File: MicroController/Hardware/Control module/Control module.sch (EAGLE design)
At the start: 90 parts, among them CN1 JST-PH_2-PIN_HEADER, CN2 JST-PH_2-PIN_HEADER, CN3 JST-PH_2-PIN_HEADER, CN4 JST-PH_2-PIN_HEADER, CN5 JST-PH_2-PIN_HEADER, CN6 JST-PH_2-PIN_HEADER, CN7 JST-PH_2-PIN_HEADER, CN8 JST-PH_2-PIN_HEADER, J1 1X2-3.5MM, J2 RJ45-TRAFO, J3 RJ45-TRAFO, J4 RJ45-TRAFO, J6 RJ11, Q1 BSS138, Q2 BSS138, Q3 BSS138, Q4 BSS138, Q5 BSS138, Q6 BSS138, Q7 BSS138, Q8 BSS138, U1 CD74HC4067SM96, U2 DUAL-OPTOISOLATOR_SOIC8, U3 TLV1117-33CDCY, U4 DUAL-OPTOISOLATOR_SOIC8

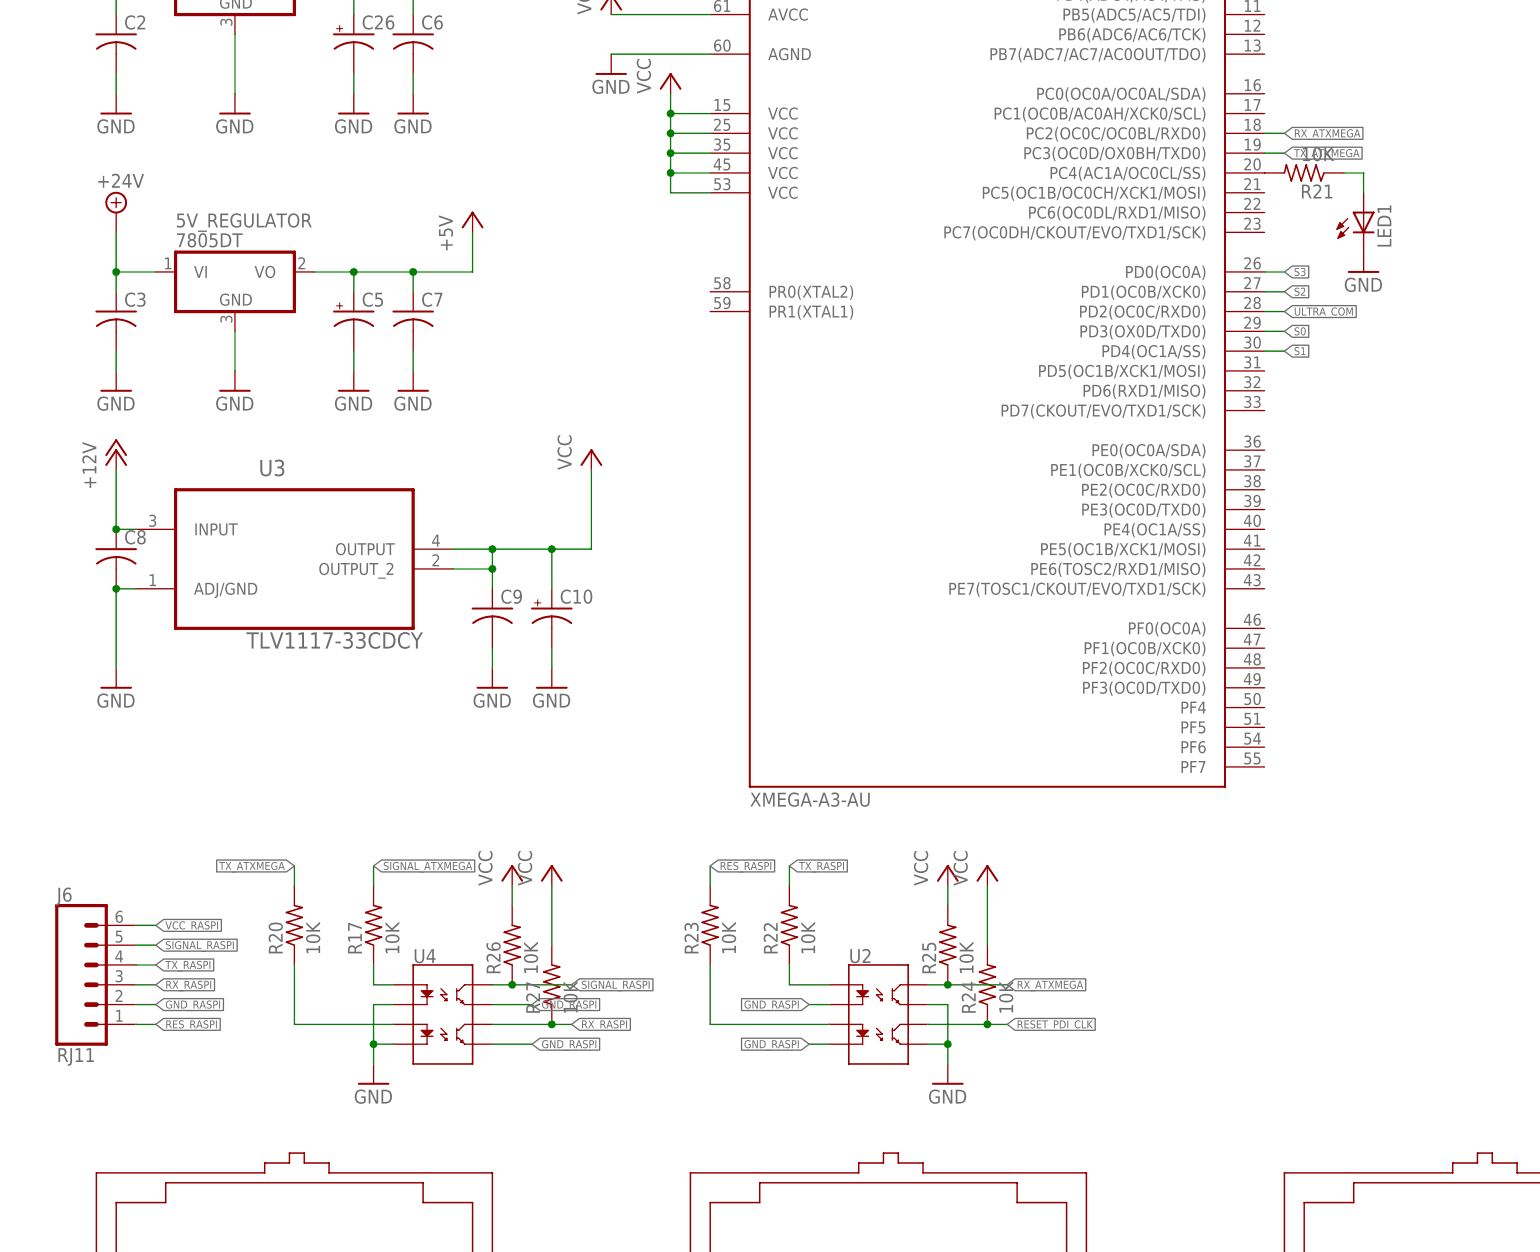
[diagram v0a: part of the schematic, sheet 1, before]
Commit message: Added the possibility for remote programming.
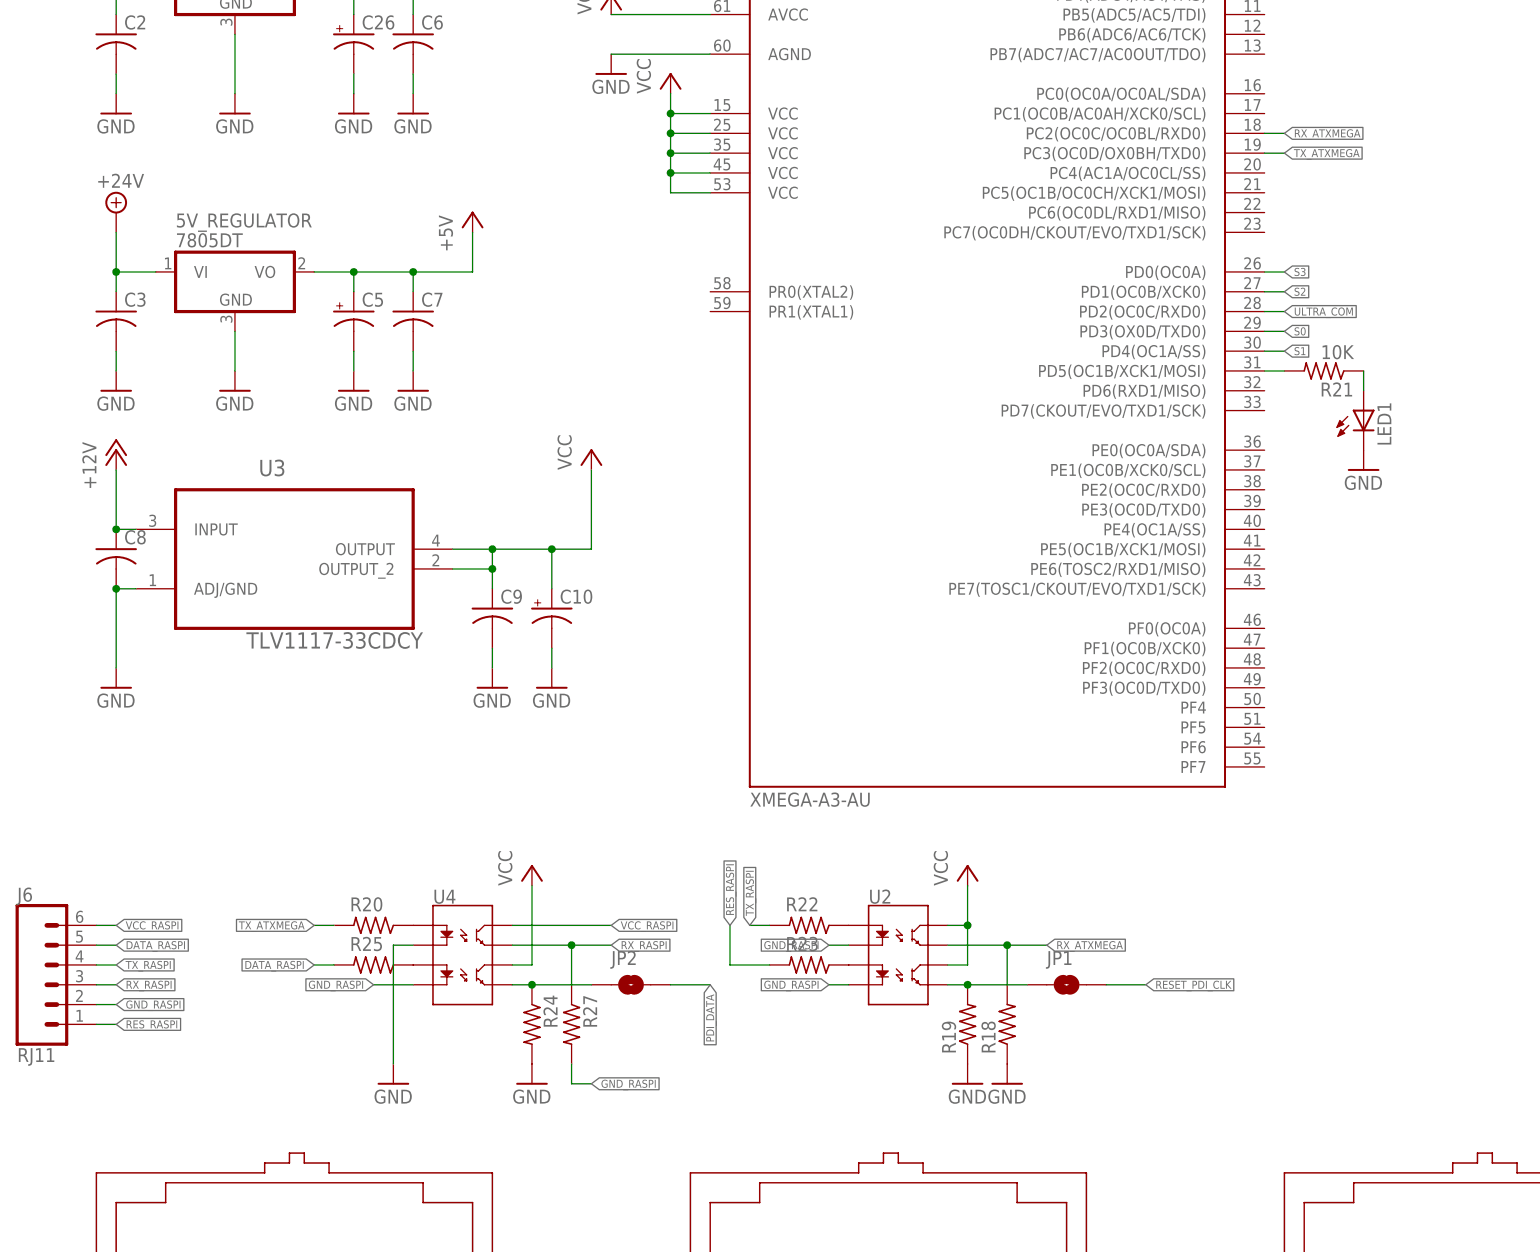
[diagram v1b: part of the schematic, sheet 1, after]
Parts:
- removed R17, R26: 10K, adafruit:R-US_R0805
- added JP1, JP2: JUMPER-SMT_2_NO_NO-SILK, SparkFun-Jumpers:JUMPER-SMT_2_NO_NO-SILK
- added R18, R19: 10K, adafruit:R-US_R0805
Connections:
- removed net N$3 (its old number): R21.2, U$1.PC4(AC1A/OC0CL/SS)
- removed net SIGNAL_ATXMEGA: R17.2
- removed net SIGNAL_RASPI: J6.5, R26.1, U4.CL1
- new net DATA_RASPI: J6.5, R25.2
- new net N$1: R21.2, U$1.PD5(OC1B/XCK1/MOSI)
- new net N$4: R20.1, U4.A1
- new net N$5: R25.1, U4.A2
- net GND: now also R18.1, R19.1, R24.2; no longer U2.EM1, U2.EM2, U4.C2
- net GND_RASPI: now also R27.2, U4.C2; no longer U4.EM1, U4.EM2
- net N$2: now also JP1.1, R19.2, U2.EM2; no longer R17.1, U4.A1
- net N$8: now also JP2.1, R24.1, U4.EM2; no longer R20.1, U4.A2
- net PDI_DATA: now also JP2.2
- net RESET_PDI_CLK: now also JP1.2; no longer R24.1, U2.CL2
- net RX_ATXMEGA: now also R18.2, U2.EM1; no longer R25.1, U2.CL1
- net RX_RASPI: now also U4.EM1; no longer U4.CL2
- net VCC: now also U2.CL1, U2.CL2, U4.CL2; no longer R24.2, R25.2, R26.2, R27.2
- net VCC_RASPI: now also U4.CL1
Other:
- moved on the sheet: J6, LED1, R20, R21, R22, R23, R24, R25, R27, U2, U4

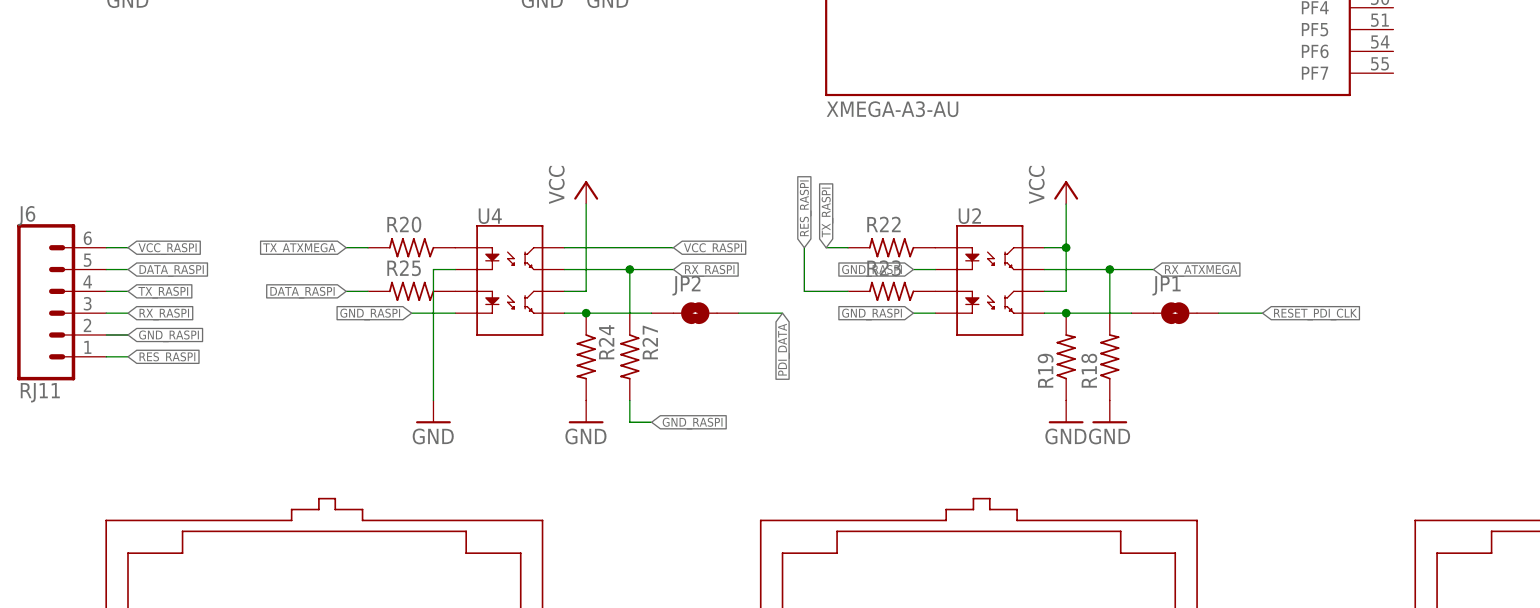
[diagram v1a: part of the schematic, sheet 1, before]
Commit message: New project for the ultrasone sensor PCB.
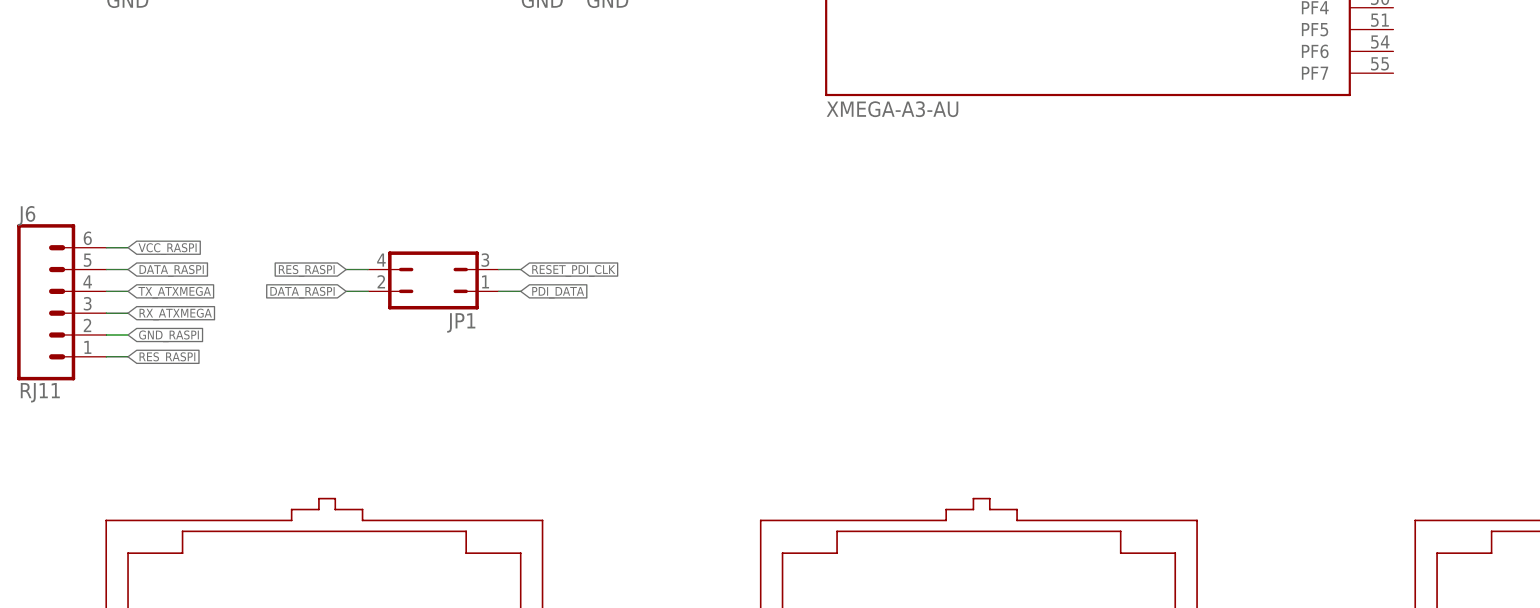
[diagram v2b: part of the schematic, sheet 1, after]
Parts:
- removed JP2: JUMPER-SMT_2_NO_NO-SILK, SparkFun-Jumpers:JUMPER-SMT_2_NO_NO-SILK
- removed R18, R19, R20, R22, R23, R24, R25, R27: 10K, adafruit:R-US_R0805
- removed U2, U4: DUAL-OPTOISOLATOR_SOIC8, SparkFun-DiscreteSemi:DUAL-OPTOISOLATOR_SOIC8
- JP1: value JUMPER-SMT_2_NO_NO-SILK -> (none); device SparkFun-Jumpers:JUMPER-SMT_2_NO_NO-SILK -> jumper:JP2Q
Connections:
- removed net N$2: JP1.1, R19.2, U2.EM2
- removed net N$4: R20.1, U4.A1
- removed net N$5: R25.1, U4.A2
- removed net N$6: R22.1, U2.A1
- removed net N$7: R23.1, U2.A2
- removed net N$8: JP2.1, R24.1, U4.EM2
- removed net RX_RASPI: J6.3, R27.1, U4.EM1
- removed net TX_RASPI: J6.4, R22.2
- net DATA_RASPI: now also JP1.2; no longer R25.2
- net GND: no longer R18.1, R19.1, R24.2, U4.C1
- net GND_RASPI: no longer R27.2, U2.C1, U2.C2, U4.C2
- net PDI_DATA: now also JP1.1; no longer JP2.2
- net RESET_PDI_CLK: now also JP1.3; no longer JP1.2
- net RES_RASPI: now also JP1.4; no longer R23.2
- net RX_ATXMEGA: now also J6.3; no longer R18.2, U2.EM1
- net TX_ATXMEGA: now also J6.4; no longer R20.2
- net VCC: no longer U2.CL1, U2.CL2, U4.CL2
- net VCC_RASPI: no longer U4.CL1

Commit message: Changed the layout drastically, especially the multiplexer.
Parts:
- removed 5V_REGULATOR: 7805DT, adafruit:7805DT
- added IC1: MCP1703CB, linear:MCP1703CB
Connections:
- net +12V: now also C25.1, C3.1, IC1.VI, J2.GND
- net +24V: no longer 5V_REGULATOR.VI, C3.1
- net +5V: now also IC1.VO; no longer 5V_REGULATOR.VO, C25.1, J2.TX+
- net GND: now also IC1.GND; no longer 5V_REGULATOR.GND, J2.GND
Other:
- moved on the sheet: C25
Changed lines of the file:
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@@
 <part name="P+15" library="supply1" library_urn="urn:adsk.eagle:library:371" deviceset="VCC" device=""/>
 <part name="12V_REGULATOR" library="adafruit" library_urn="urn:adsk.eagle:library:420" deviceset="78*" device="DT" technology="12"/>
-<part name="5V_REGULATOR" library="adafruit" library_urn="urn:adsk.eagle:library:420" deviceset="78*" device="DT" technology="05"/>
 <part name="P+2" library="supply1" library_urn="urn:adsk.eagle:library:371" deviceset="+12V" device=""/>
 <part name="P+4" library="supply1" library_urn="urn:adsk.eagle:library:371" deviceset="+12V" device=""/>
@@
 <part name="GND4" library="supply1" library_urn="urn:adsk.eagle:library:371" deviceset="GND" device=""/>
 <part name="GND5" library="supply1" library_urn="urn:adsk.eagle:library:371" deviceset="GND" device=""/>
-<part name="SUPPLY3" library="supply2" library_urn="urn:adsk.eagle:library:372" deviceset="+24V" device=""/>
 <part name="GND6" library="supply1" library_urn="urn:adsk.eagle:library:371" deviceset="GND" device=""/>
 <part name="GND7" library="supply1" library_urn="urn:adsk.eagle:library:371" deviceset="GND" device=""/>
@@
 <part name="P+39" library="supply1" library_urn="urn:adsk.eagle:library:371" deviceset="+5V" device=""/>
 <part name="P+40" library="supply1" library_urn="urn:adsk.eagle:library:371" deviceset="+5V" device=""/>
-<part name="P+41" library="supply1" library_urn="urn:adsk.eagle:library:371" deviceset="+5V" device=""/>
 <part name="C23" library="adafruit" library_urn="urn:adsk.eagle:library:420" deviceset="C-US" device="C0805"/>
 <part name="GND51" library="supply1" library_urn="urn:adsk.eagle:library:371" deviceset="GND" device=""/>
@@
 <part name="C1" library="adafruit" library_urn="urn:adsk.eagle:library:420" deviceset="CPOL-US" device="175TMP-0810"/>
 <part name="JP1" library="jumper" library_urn="urn:adsk.eagle:library:252" deviceset="JP2Q" device="" package3d_urn="urn:adsk.eagle:package:15450/1"/>
+<part name="IC1" library="linear" library_urn="urn:adsk.eagle:library:262" deviceset="MCP1703" device="CB" package3d_urn="urn:adsk.eagle:package:16489/2"/>
+<part name="P+38" library="supply1" library_urn="urn:adsk.eagle:library:371" deviceset="+12V" device=""/>
+<part name="P+41" library="supply1" library_urn="urn:adsk.eagle:library:371" deviceset="+12V" device=""/>
 </parts>
 <sheets>
@@
 <instance part="P+15" gate="VCC" x="337.82" y="10.16"/>
 <instance part="12V_REGULATOR" gate="A1" x="17.78" y="170.18"/>
-<instance part="5V_REGULATOR" gate="A1" x="17.78" y="132.08"/>
 <instance part="P+2" gate="1" x="302.26" y="93.98"/>
 <instance part="P+4" gate="1" x="353.06" y="93.98"/>
@@
 <instance part="GND4" gate="1" x="2.54" y="152.4"/>
 <instance part="GND5" gate="1" x="17.78" y="152.4"/>
-<instance part="SUPPLY3" gate="+24V" x="2.54" y="139.7"/>
 <instance part="GND6" gate="1" x="17.78" y="116.84"/>
 <instance part="GND7" gate="1" x="2.54" y="116.84"/>
@@
 <instance part="P+39" gate="1" x="2.54" y="-10.16"/>
 <instance part="P+40" gate="1" x="78.74" y="-10.16"/>
-<instance part="P+41" gate="1" x="154.94" y="-10.16"/>
 <instance part="C23" gate="G$1" x="7.62" y="-20.32"/>
 <instance part="GND51" gate="1" x="7.62" y="-30.48"/>
 <instance part="C24" gate="G$1" x="83.82" y="-20.32"/>
 <instance part="GND52" gate="1" x="83.82" y="-30.48"/>
-<instance part="C25" gate="G$1" x="160.02" y="-20.32"/>
+<instance part="C25" gate="G$1" x="195.58" y="-20.32"/>
 <instance part="GND53" gate="1" x="160.02" y="-30.48"/>
 <instance part="CN1" gate="G$1" x="210.82" y="152.4" smashed="yes" rot="R90">
@@
 <instance part="C1" gate="G$1" x="35.56" y="195.58"/>
 <instance part="JP1" gate="B1" x="38.1" y="43.18" rot="R90"/>
+<instance part="IC1" gate="G$1" x="17.78" y="132.08"/>
+<instance part="P+38" gate="1" x="2.54" y="139.7"/>
+<instance part="P+41" gate="1" x="203.2" y="-12.7"/>
 </instances>
 <busses>
@@
 </segment>
 <segment>
-<pinref part="5V_REGULATOR" gate="A1" pin="GND"/>
 <pinref part="GND6" gate="1" pin="GND"/>
 <wire x1="17.78" y1="124.46" x2="17.78" y2="119.38" width="0.1524" layer="91"/>
+<pinref part="IC1" gate="G$1" pin="GND"/>
 </segment>
 <segment>
@@
 </segment>
 <segment>
-<pinref part="GND23" gate="1" pin="GND"/>
-<pinref part="J2" gate="G$1" pin="GND"/>
-<wire x1="195.58" y1="-27.94" x2="195.58" y2="-12.7" width="0.1524" layer="91"/>
-</segment>
-<segment>
 <pinref part="GND32" gate="1" pin="GND"/>
 <pinref part="U$1" gate="G$1" pin="AGND"/>
@@
 </segment>
 <segment>
-<pinref part="GND53" gate="1" pin="GND"/>
-<pinref part="C25" gate="G$1" pin="2"/>
-<wire x1="160.02" y1="-27.94" x2="160.02" y2="-25.4" width="0.1524" layer="91"/>
-</segment>
-<segment>
 <pinref part="CN1" gate="G$1" pin="1"/>
 <pinref part="GND54" gate="1" pin="GND"/>
@@
 <pinref part="CN8" gate="G$1" pin="1"/>
 <pinref part="GND61" gate="1" pin="GND"/>
+</segment>
+<segment>
+<pinref part="GND23" gate="1" pin="GND"/>
+<pinref part="C25" gate="G$1" pin="2"/>
+<wire x1="195.58" y1="-27.94" x2="195.58" y2="-25.4" width="0.1524" layer="91"/>
 </segment>
 </net>
@@
 <junction x="2.54" y="99.06"/>
 </segment>
+<segment>
+<wire x1="7.62" y1="132.08" x2="2.54" y2="132.08" width="0.1524" layer="91"/>
+<wire x1="2.54" y1="132.08" x2="2.54" y2="137.16" width="0.1524" layer="91"/>
+<pinref part="C3" gate="G$1" pin="1"/>
+<wire x1="2.54" y1="129.54" x2="2.54" y2="132.08" width="0.1524" layer="91"/>
+<junction x="2.54" y="132.08"/>
+<pinref part="IC1" gate="G$1" pin="VI"/>
+<pinref part="P+38" gate="1" pin="+12V"/>
+</segment>
+<segment>
+<pinref part="C25" gate="G$1" pin="1"/>
+<pinref part="J2" gate="G$1" pin="GND"/>
+<wire x1="195.58" y1="-17.78" x2="195.58" y2="-15.24" width="0.1524" layer="91"/>
+<pinref part="P+41" gate="1" pin="+12V"/>
+<wire x1="195.58" y1="-15.24" x2="195.58" y2="-12.7" width="0.1524" layer="91"/>
+<wire x1="203.2" y1="-15.24" x2="195.58" y2="-15.24" width="0.1524" layer="91"/>
+<junction x="195.58" y="-15.24"/>
+</segment>
 </net>
 <net name="VIN" class="0">
@@
 <junction x="2.54" y="170.18"/>
 </segment>
-<segment>
-<pinref part="5V_REGULATOR" gate="A1" pin="VI"/>
-<pinref part="SUPPLY3" gate="+24V" pin="+24V"/>
-<wire x1="7.62" y1="132.08" x2="2.54" y2="132.08" width="0.1524" layer="91"/>
-<wire x1="2.54" y1="132.08" x2="2.54" y2="137.16" width="0.1524" layer="91"/>
-<pinref part="C3" gate="G$1" pin="1"/>
-<wire x1="2.54" y1="129.54" x2="2.54" y2="132.08" width="0.1524" layer="91"/>
-<junction x="2.54" y="132.08"/>
-</segment>
 </net>
 <net name="+5V" class="0">
 <segment>
 <pinref part="P+18" gate="1" pin="+5V"/>
-<pinref part="5V_REGULATOR" gate="A1" pin="VO"/>
 <wire x1="48.26" y1="137.16" x2="48.26" y2="132.08" width="0.1524" layer="91"/>
 <wire x1="48.26" y1="132.08" x2="40.64" y2="132.08" width="0.1524" layer="91"/>
@@
 <wire x1="40.64" y1="129.54" x2="40.64" y2="132.08" width="0.1524" layer="91"/>
 <junction x="40.64" y="132.08"/>
+<pinref part="IC1" gate="G$1" pin="VO"/>
 </segment>
 <segment>
@@
 <junction x="83.82" y="-15.24"/>
 </segment>
-<segment>
-<pinref part="P+41" gate="1" pin="+5V"/>
-<wire x1="154.94" y1="-12.7" x2="154.94" y2="-15.24" width="0.1524" layer="91"/>
-<pinref part="C25" gate="G$1" pin="1"/>
-<pinref part="J2" gate="G$1" pin="TX+"/>
-<wire x1="160.02" y1="-17.78" x2="160.02" y2="-15.24" width="0.1524" layer="91"/>
-<wire x1="160.02" y1="-15.24" x2="160.02" y2="-12.7" width="0.1524" layer="91"/>
-<wire x1="154.94" y1="-15.24" x2="160.02" y2="-15.24" width="0.1524" layer="91"/>
-<junction x="160.02" y="-15.24"/>
-</segment>
-</net>
+</net>
